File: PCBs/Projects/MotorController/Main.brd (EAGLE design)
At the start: 172.7 x 138.1 mm, 115 parts, among them Q1 ZXMP10A17GQ, Q2 MMBT5551LT1G, Q3 BUK9240-100A.118, Q4 BUK9240-100A.118, U1 DRV8301, U11 LT4356-2, U2 ESDA6V1SC6Y, U3 ESDA6V1SC6Y, U4 TMP101, U5 ACS758LCB, U6 ESDA6V1SC6Y, U7 MTI85W100GC

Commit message: Lots more layout complete -major micro controller rewiring -removed a connector and replaced it with a header -added some datasheets for cykit
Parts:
- removed J4: (no value), connectorsTVD:2X03_MINIFIT_JR
- removed MOD1: PSOC5LP-DEVBRDCY8CKIT-059, modules:CYKIT059
- removed R26, R27, R28: 100, SparkFun-Resistors:0805
- added J6: (no value), SparkFun-Connectors:1X06
- added MOD2: PSOC5LP-DEVBRDCY8CKIT-059, modules:CYKIT059
- added R42, R44, R45, R46, R47: 100, SparkFun-Resistors:0805
- added SJ4: SOLDERJUMPERTRACE, SparkFun-Retired:SJ_2S-TRACE
- added U8: ESDA6V1SC6Y, IC:SOT23-6
- moved R32 293.3 mm to (143.8, 43.4)
- moved R33 286.7 mm to (148.0, 33.9), turned to 180 degrees
- moved C28 244.6 mm to (122.0, 107.1)
- moved C26 241.4 mm to (128.3, 118.4)
- moved C25 241.0 mm to (131.4, 116.5)
- moved C27 241.0 mm to (123.7, 115.8), turned to 90 degrees
- moved R38 237.0 mm to (124.6, 119.5)
- moved C24 236.9 mm to (88.4, 44.7)
- moved R37 230.0 mm to (121.4, 120.1)
- moved R36 226.0 mm to (120.7, 116.6), turned to 90 degrees
- moved D8 213.9 mm to (132.8, 77.0), turned to 180 degrees
- moved D7 212.7 mm to (115.6, 66.3), turned to 180 degrees
- moved D6 211.3 mm to (43.4, 56.4), turned to 270 degrees
- moved D9 202.8 mm to (133.6, 64.8), turned to 180 degrees
- moved R31 202.2 mm to (144.0, 34.0)
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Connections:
- removed net N$27: MOD1.10, R26.2
- removed net N$28: MOD1.11, R27.2
- removed net N$29: MOD1.12, R28.2
- new net N$16: MOD2.30, R42.2
- new net N$45: SJ4.2, U1.4
- new net N$47: MOD2.11, R45.2
- new net N$48: MOD2.12, R46.2
- new net N$49: MOD2.23, R47.2
- new net N$8: MOD2.10, R44.2
- net !CS: now also MOD2.45; no longer MOD1.36
- net !FAULT: now also MOD2.49; no longer MOD1.44
- net !OCTW: now also MOD2.50; no longer MOD1.43
- net 5V: now also J6.1, MOD2.26, MOD2.52; no longer J4.5, MOD1.26, MOD1.52
- net DISABLE: now also R42.1, U2.6
- net DISP_OUT: now also J6.4; no longer J4.6
- net EN_GATE: now also MOD2.40; no longer MOD1.45
- net GND: now also J2.5, J6.6, MOD2.1, MOD2.25, MOD2.51, U8.2, U8.5; no longer J4.2, MOD1.1, MOD1.25, MOD1.51
- net GPIO_TBD: now also J6.5; no longer J4.4
- net H1: now also R44.1, U6.3; no longer R26.1
- net H2: now also R45.1, U6.4; no longer R27.1
- net H3: now also R46.1, U6.6; no longer R28.1
- net INH_A: now also MOD2.39; no longer MOD1.49
- net INH_B: now also MOD2.37; no longer MOD1.27
- net INH_C: now also MOD2.35; no longer MOD1.29
- net INL_A: now also MOD2.38; no longer MOD1.50
- net INL_B: now also MOD2.36; no longer MOD1.28
- net INL_C: now also MOD2.34; no longer MOD1.30
- net ISENSE: now also MOD2.3, U8.4; no longer MOD1.3, U2.6
- net MISO: now also MOD2.47; no longer MOD1.38
- net MONITOR_RX: now also J6.3; no longer J4.3
- net MONITOR_TX: now also J6.2; no longer J4.1
- net MOSI: now also MOD2.46; no longer MOD1.39
- net N$32: now also MOD2.33; no longer MOD1.34
- net N$33: now also MOD2.32; no longer MOD1.33
- net N$34: now also MOD2.31; no longer MOD1.32
- net N$39: now also MOD2.6; no longer MOD1.6
- net N$41: now also MOD2.29; no longer MOD1.47
- net N$42: now also MOD2.22; no longer MOD1.46
- net N$43: now also MOD2.13; no longer MOD1.14
- net N$44: now also MOD2.15; no longer MOD1.15
- net PWRGD: now also MOD2.24, SJ4.1; no longer U1.4
- net REVERSE: now also R47.1, U2.4
- net SCL: now also MOD2.8; no longer MOD1.42
- net SCLK: now also MOD2.48; no longer MOD1.37
- net SDA: now also MOD2.9; no longer MOD1.41
- net T_ALERT: now also MOD2.21; no longer MOD1.40
- net VSENSE: now also MOD2.2, U8.1; no longer MOD1.2, U2.4
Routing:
- net REVERSE: track 0.00 -> 144.6 mm, vias 0 -> 2
- net VSENSE: track 0.00 -> 80.2 mm, vias 0 -> 2
- net N$42: track 0.00 -> 71.9 mm, vias 0 -> 2
- net N$41: track 0.00 -> 71.9 mm, vias 0 -> 2
- net N$45: track 0.00 -> 59.2 mm, vias 0 -> 2
- net N$44: track 0.00 -> 50.4 mm, vias 0 -> 2
- net N$43: track 0.00 -> 43.0 mm, vias 0 -> 2
- net SCLK: track 0.00 -> 42.5 mm
- net MISO: track 0.00 -> 41.7 mm
- net !OCTW: track 0.00 -> 36.9 mm
- net BUCK-EN: track 2.80 -> 38.5 mm, vias 1 -> 2
- net ISENSE: track 0.00 -> 33.5 mm
- net !FAULT: track 0.00 -> 32.0 mm
- net MOSI: track 0.00 -> 31.8 mm
- net !CS: track 0.00 -> 31.4 mm
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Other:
- board size 172.7 x 138.1 mm -> 172.7 x 128.3 mm

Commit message: First pass layout complete -still need to go over it with a fine toothed comb
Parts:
- removed FD1, FD3, FD5: FIDUCIAL1X2, SparkFun-Aesthetics:FIDUCIAL-1X2
- moved S6 119.9 mm to (5.08, 87.0)
- moved FD2 110.8 mm to (127.8, 90.3)
- moved FD4 89.0 mm to (5.84, 82.0)
- moved D12 50.5 mm to (121.7, 20.1), turned to 270 degrees
- moved D10 46.1 mm to (121.7, 31.0), turned to 270 degrees
- moved FD6 43.8 mm to (6.48, 5.21)
- moved R25 43.7 mm to (10.9, 61.1), turned to 90 degrees
- moved C28 40.8 mm to (109.7, 68.2), turned to 180 degrees
- moved D11 40.4 mm to (130.4, 20.1), turned to 90 degrees
- moved R38 38.6 mm to (134.5, 82.2), turned to 90 degrees
- moved D8 36.8 mm to (121.7, 41.9), turned to 270 degrees
- moved R37 36.7 mm to (134.5, 85.9), turned to 90 degrees
- moved C27 36.2 mm to (136.9, 82.2)
- moved R41 35.4 mm to (47.6, 6.86), turned to 270 degrees
- moved S1 35.4 mm to (41.3, 6.99)
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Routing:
- net 5V: track 0.00 -> 479.5 mm, vias 0 -> 12
- net THROTTLE_2: track 0.00 -> 218.0 mm, vias 0 -> 3
- net H2: track 0.00 -> 193.7 mm, vias 0 -> 7
- net H1: track 0.00 -> 186.5 mm, vias 0 -> 4
- net H3: track 0.00 -> 181.3 mm, vias 0 -> 6
- net SCL: track 0.00 -> 134.5 mm, vias 0 -> 2
- net SDA: track 0.00 -> 129.9 mm, vias 0 -> 2
- net DISABLE: track 6.23 -> 124.9 mm, vias 0 -> 4
- net T_ALERT: track 0.00 -> 103.2 mm, vias 0 -> 4
- net ISENSE: track 33.5 -> 120.4 mm, vias 0 -> 3
- net A: track 37.5 -> 80.0 mm
- net B: track 29.7 -> 69.5 mm
- net C: track 31.2 -> 68.8 mm
- net REVERSE: track 144.6 -> 175.4 mm
- net N$16: track 6.47 -> 18.5 mm
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- added copper zone on layer 1, net A
- added copper zone on layer 1, net B
- added copper zone on layer 1, net C
- added copper zone on layer 1, net GND
- added copper zone on layer 16, net GND
- added copper zone on layer 16, net VCC
- added copper zone on layer 1, net VIN
- added copper zone on layer 1, net V_BATT
- added copper zone on layer 16, net V_BATT
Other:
- board size 172.7 x 128.3 mm -> 172.7 x 95.2 mm

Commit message: fixed a couple airwires -Added keepout below 1206 resistors -TODO: current path from power input to fets needs to bet larger -TODO: silk screen fixes -TODO: DRV8301 solder mask fix -TODO: Mounting hole placement -TODO: interior layer placement
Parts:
- removed S2, S3, S4, S5: STANDOFF_ELECTRICAL, SparkFun-Electromechanical:STANDOFF-ELECTRICAL
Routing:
- net VCC: track 14.8 -> 39.0 mm
- net GND: track 116.2 -> 125.1 mm, vias 54 -> 82
- net PREJUMP_5V: track 8.68 -> 0.90 mm
- net 5V: track 479.5 -> 472.7 mm
- net B: track 69.5 -> 71.3 mm
- net DISABLE: track 124.9 -> 126.5 mm
- added copper zone on layer 1, net 5V
- added copper zone on layer 1, net PREJUMP_5V
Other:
- board size 172.7 x 95.2 mm -> 172.7 x 99.1 mm

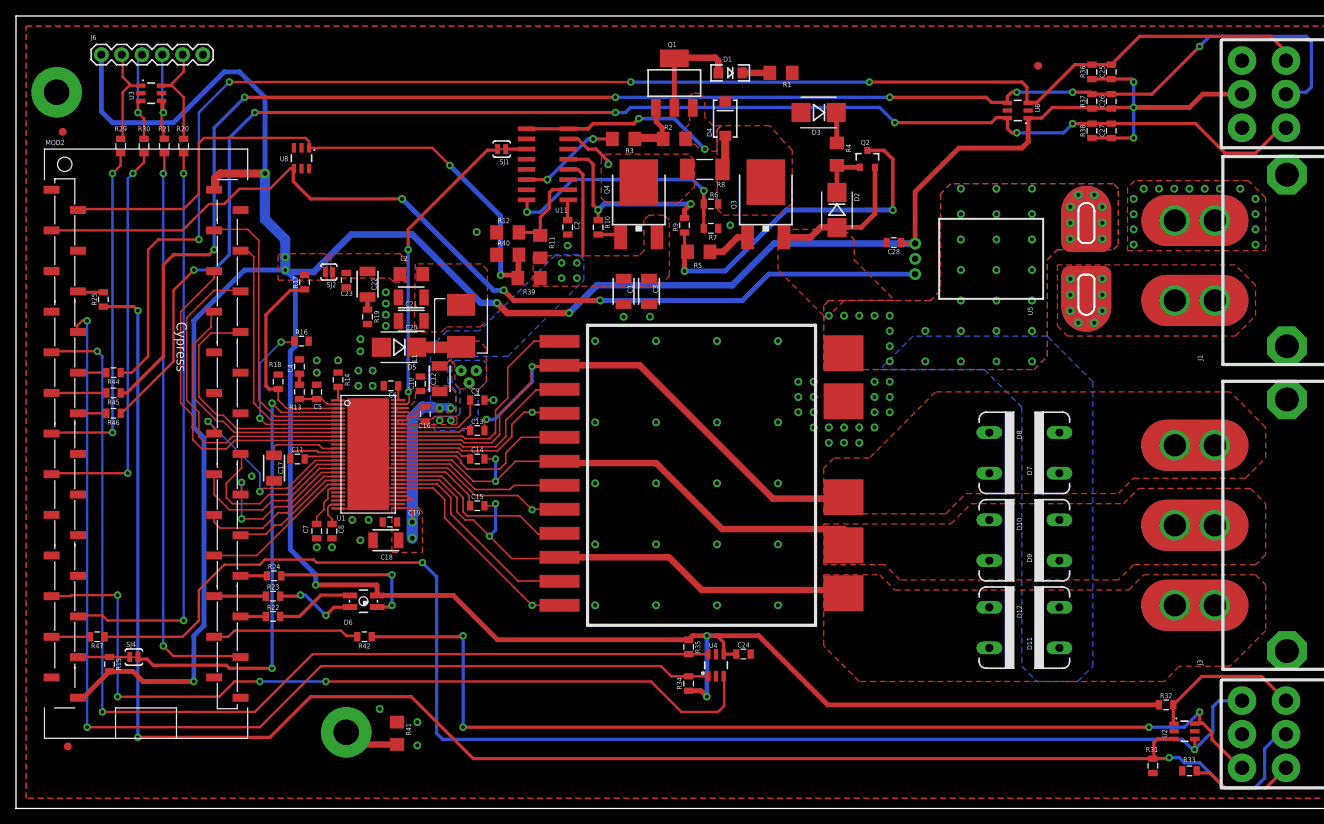
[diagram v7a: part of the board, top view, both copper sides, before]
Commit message: Fixed current path concerns -Arranged top fiducials
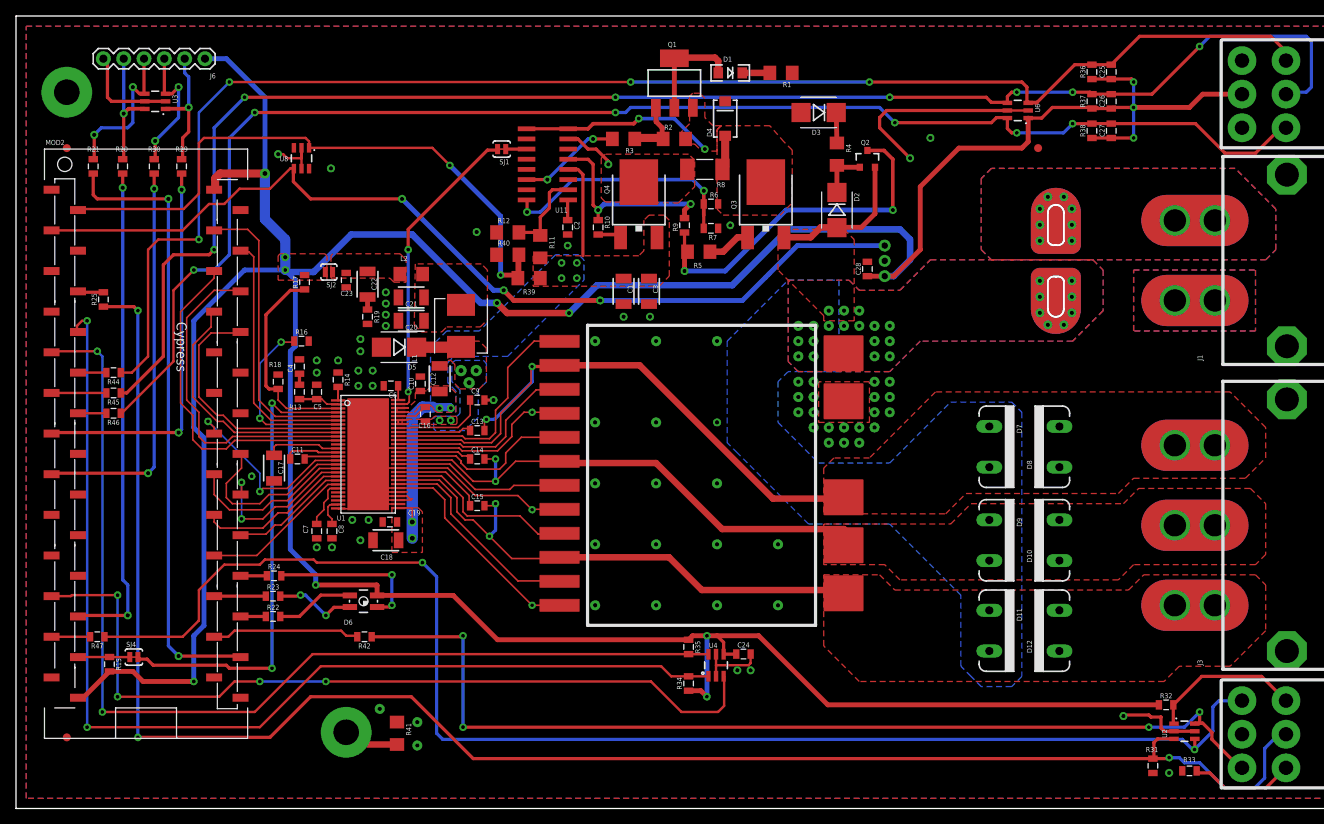
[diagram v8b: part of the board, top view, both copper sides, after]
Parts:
- moved J6 13.0 mm to (23.6, 91.2), turned to 180 degrees
- moved FD2 10.3 mm to (127.8, 80.0)
- moved R21 9.25 mm to (9.65, 77.7)
- moved D7 8.80 mm to (121.7, 42.7), turned to 270 degrees
- moved D8 8.80 mm to (130.4, 42.7), turned to 90 degrees
- moved D11 8.77 mm to (121.7, 19.7), turned to 270 degrees
- moved D12 8.77 mm to (130.4, 19.7), turned to 90 degrees
- moved D10 8.76 mm to (130.4, 31.0), turned to 90 degrees
- moved D9 8.76 mm to (121.7, 31.0), turned to 270 degrees
- moved R29 8.03 mm to (20.7, 77.7)
- moved R20 8.03 mm to (13.3, 77.7)
- moved C28 4.67 mm to (106.4, 64.9), turned to 90 degrees
- moved U5 3.82 mm to (108.6, 65.9), flipped to the bottom, turned to 90 degrees
- moved R30 2.84 mm to (17.3, 77.7)
- moved FD4 2.09 mm to (6.35, 80.0)
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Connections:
- net GND: now also J1.1_1, J1.1_2; no longer J1.2_1, J1.2_2
- net VIN: now also J1.2_1, J1.2_2; no longer J1.1_1, J1.1_2
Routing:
- net GND: track 125.1 -> 189.1 mm, vias 82 -> 72
- net N$42: track 71.9 -> 61.8 mm
- net 5V: track 472.7 -> 464.0 mm
- net MONITOR_TX: track 12.9 -> 19.1 mm, vias 0 -> 1
- net N$41: track 71.9 -> 77.7 mm
- net DISP_OUT: track 13.7 -> 19.3 mm, vias 1 -> 2
- net N$43: track 43.0 -> 48.5 mm
- net GPIO_TBD: track 14.3 -> 18.4 mm, vias 0 -> 1
- net MONITOR_RX: track 13.3 -> 16.7 mm, vias 1 -> 2
- net ISENSE: track 120.4 -> 118.1 mm
- net N$44: track 50.4 -> 49.9 mm
- net V_BATT: vias 31 -> 18
- added copper zone on layer 16, net VIN
